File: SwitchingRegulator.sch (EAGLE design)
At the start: 31 parts, among them J1 APP_2POS_CONFIG5V_HORIZ, J2 APP_2POS_CONFIG5V_HORIZ, J3 APP_2POS_CONFIG5V_HORIZ, Q1 Q_OKI-78SR, Q2 Q_CSD18532KCSPCB

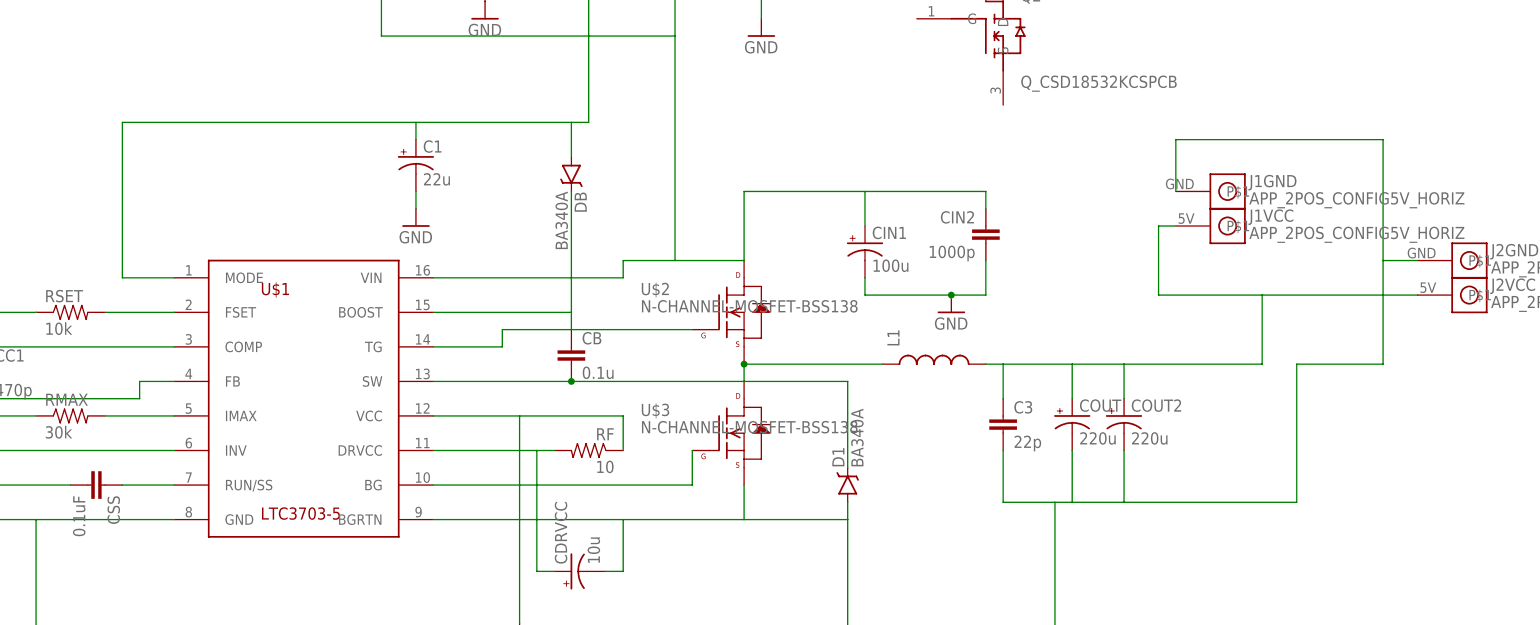
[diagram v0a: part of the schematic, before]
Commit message: Updated a few components
COUT 1, COUT 2, CIN1, and C1 now correspond to their true package
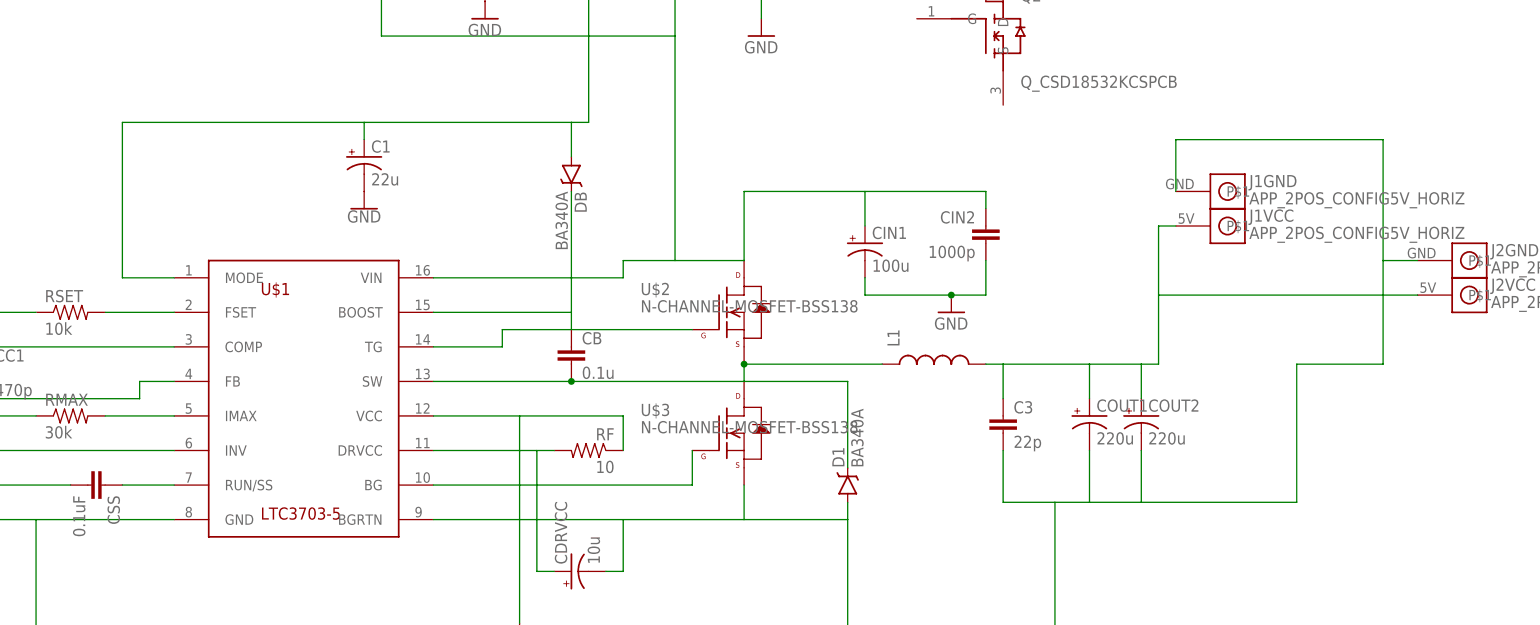
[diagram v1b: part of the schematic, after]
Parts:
- removed COUT: 220u, SparkFun-Passives:CAP_POL1206
- added COUT1: 220u, MRDT-2015-PowerBoard:EGPD101ELL221MK25H
- C1: device SparkFun-Passives:CAP_POL1206 -> buckconverter:UCZ1K220MCL1GS
- CIN1: device SparkFun-Passives:CAP_POL1206 -> MRDT-2015-PowerBoard:B41858C9107M000
- COUT2: device SparkFun-Passives:CAP_POL1206 -> MRDT-2015-PowerBoard:EGPD101ELL221MK25H
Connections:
- net GND: now also C1.-, COUT1.-; no longer COUT.-
- net VOUT12+: now also COUT1.+; no longer COUT.+
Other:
- moved on the sheet: C1, COUT2
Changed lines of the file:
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@@
 <part name="RF" library="SparkFun-Passives" deviceset="RESISTOR" device="0603-RES" value="10"/>
 <part name="GND1" library="SparkFun-Aesthetics" deviceset="GND" device=""/>
-<part name="GND2" library="SparkFun-Aesthetics" deviceset="GND" device=""/>
 <part name="GND3" library="SparkFun-Aesthetics" deviceset="GND" device=""/>
-<part name="CIN1" library="SparkFun-Passives" deviceset="CAP_POL" device="1206" value="100u"/>
-<part name="C1" library="SparkFun-Passives" deviceset="CAP_POL" device="1206" value="22u"/>
 <part name="CDRVCC" library="SparkFun-Passives" deviceset="CAP_POL" device="1206" value="10u"/>
-<part name="COUT" library="SparkFun-Passives" deviceset="CAP_POL" device="1206" value="220u"/>
-<part name="COUT2" library="SparkFun-Passives" deviceset="CAP_POL" device="1206" value="220u"/>
 <part name="GND4" library="SparkFun-Aesthetics" deviceset="GND" device=""/>
 <part name="Q1" library="MRDT-2014-All" deviceset="Q_OKI-78SR" device=""/>
@@
 <part name="J3" library="MRDT-Connectors" deviceset="APP_2POS_CONFIG" device="5V_HORIZ"/>
 <part name="Q2" library="MRDT-2014-All" deviceset="Q_CSD18532KCS" device="PCB"/>
+<part name="COUT1" library="MRDT-2015-PowerBoard" deviceset="EGPD101ELL221MK25H" device="" value="220u"/>
+<part name="COUT2" library="MRDT-2015-PowerBoard" deviceset="EGPD101ELL221MK25H" device="" value="220u"/>
+<part name="CIN1" library="MRDT-2015-PowerBoard" deviceset="B41858C9107M000" device="" value="100u"/>
+<part name="C1" library="buckconverter" deviceset="UCZ1K220MCL1GS" device="" value="22u"/>
+<part name="GND2" library="SparkFun-PowerSymbols" library_urn="urn:adsk.eagle:library:530" deviceset="GND" device=""/>
 </parts>
 <sheets>
@@
 <instance part="RF" gate="G$1" x="127" y="109.22" rot="MR0"/>
 <instance part="GND1" gate="1" x="30.48" y="73.66"/>
-<instance part="GND2" gate="1" x="101.6" y="142.24"/>
 <instance part="GND3" gate="1" x="180.34" y="129.54"/>
-<instance part="CIN1" gate="G$1" x="167.64" y="139.7"/>
-<instance part="C1" gate="G$1" x="101.6" y="152.4"/>
 <instance part="CDRVCC" gate="G$1" x="124.46" y="91.44" rot="R90"/>
-<instance part="COUT" gate="G$1" x="198.12" y="114.3"/>
-<instance part="COUT2" gate="G$1" x="205.74" y="114.3"/>
 <instance part="GND4" gate="1" x="152.4" y="170.18"/>
 <instance part="Q1" gate="G$1" x="111.76" y="187.96"/>
@@
 <instance part="J3" gate="VCC" x="139.7" y="195.58" rot="R90"/>
 <instance part="Q2" gate="G$1" x="187.96" y="170.18"/>
+<instance part="COUT1" gate="G$1" x="200.66" y="111.76"/>
+<instance part="COUT2" gate="G$1" x="208.28" y="111.76"/>
+<instance part="CIN1" gate="G$1" x="167.64" y="137.16"/>
+<instance part="C1" gate="G$1" x="93.98" y="149.86"/>
+<instance part="GND2" gate="1" x="93.98" y="144.78"/>
 </instances>
 <busses>
@@
 <wire x1="165.1" y1="99.06" x2="165.1" y2="76.2" width="0.1524" layer="91"/>
 <wire x1="165.1" y1="76.2" x2="116.84" y2="76.2" width="0.1524" layer="91"/>
-<pinref part="COUT2" gate="G$1" pin="-"/>
-<wire x1="205.74" y1="109.22" x2="205.74" y2="101.6" width="0.1524" layer="91"/>
-<wire x1="205.74" y1="101.6" x2="198.12" y2="101.6" width="0.1524" layer="91"/>
 <pinref part="C3" gate="G$1" pin="2"/>
-<wire x1="198.12" y1="101.6" x2="195.58" y2="101.6" width="0.1524" layer="91"/>
 <wire x1="195.58" y1="101.6" x2="187.96" y2="101.6" width="0.1524" layer="91"/>
 <wire x1="187.96" y1="101.6" x2="187.96" y2="109.22" width="0.1524" layer="91"/>
-<pinref part="COUT" gate="G$1" pin="-"/>
-<wire x1="198.12" y1="109.22" x2="198.12" y2="101.6" width="0.1524" layer="91"/>
 <wire x1="195.58" y1="101.6" x2="195.58" y2="76.2" width="0.1524" layer="91"/>
 <wire x1="195.58" y1="76.2" x2="165.1" y2="76.2" width="0.1524" layer="91"/>
@@
 <wire x1="132.08" y1="91.44" x2="132.08" y2="99.06" width="0.1524" layer="91"/>
 <wire x1="231.14" y1="121.92" x2="231.14" y2="101.6" width="0.1524" layer="91"/>
-<wire x1="231.14" y1="101.6" x2="205.74" y2="101.6" width="0.1524" layer="91"/>
+<wire x1="231.14" y1="101.6" x2="208.28" y2="101.6" width="0.1524" layer="91"/>
+<wire x1="208.28" y1="101.6" x2="200.66" y2="101.6" width="0.1524" layer="91"/>
+<wire x1="200.66" y1="101.6" x2="195.58" y2="101.6" width="0.1524" layer="91"/>
 <wire x1="231.14" y1="121.92" x2="243.84" y2="121.92" width="0.1524" layer="91"/>
 <wire x1="243.84" y1="121.92" x2="243.84" y2="137.16" width="0.1524" layer="91"/>
@@
 <wire x1="213.36" y1="154.94" x2="243.84" y2="154.94" width="0.1524" layer="91"/>
 <wire x1="243.84" y1="154.94" x2="243.84" y2="137.16" width="0.1524" layer="91"/>
-</segment>
-<segment>
-<pinref part="GND2" gate="1" pin="GND"/>
-<wire x1="101.6" y1="144.78" x2="101.6" y2="147.32" width="0.1524" layer="91"/>
+<pinref part="COUT1" gate="G$1" pin="-"/>
+<wire x1="200.66" y1="109.22" x2="200.66" y2="101.6" width="0.1524" layer="91"/>
+<pinref part="COUT2" gate="G$1" pin="-"/>
+<wire x1="208.28" y1="109.22" x2="208.28" y2="101.6" width="0.1524" layer="91"/>
 </segment>
 <segment>
@@
 <wire x1="180.34" y1="132.08" x2="167.64" y2="132.08" width="0.1524" layer="91"/>
 <junction x="180.34" y="132.08"/>
+<wire x1="167.64" y1="132.08" x2="167.64" y2="134.62" width="0.1524" layer="91"/>
 <pinref part="CIN1" gate="G$1" pin="-"/>
-<wire x1="167.64" y1="132.08" x2="167.64" y2="134.62" width="0.1524" layer="91"/>
 </segment>
 <segment>
@@
 <pinref part="Q1" gate="G$1" pin="GND"/>
 <pinref part="GND5" gate="1" pin="GND"/>
+</segment>
+<segment>
+<pinref part="C1" gate="G$1" pin="-"/>
+<pinref part="GND2" gate="1" pin="GND"/>
 </segment>
 </net>
@@
 <wire x1="66.04" y1="134.62" x2="58.42" y2="134.62" width="0.1524" layer="91"/>
 <wire x1="58.42" y1="134.62" x2="58.42" y2="157.48" width="0.1524" layer="91"/>
-<wire x1="58.42" y1="157.48" x2="101.6" y2="157.48" width="0.1524" layer="91"/>
-<pinref part="C1" gate="G$1" pin="+"/>
-<wire x1="101.6" y1="157.48" x2="124.46" y2="157.48" width="0.1524" layer="91"/>
-<wire x1="101.6" y1="154.94" x2="101.6" y2="157.48" width="0.1524" layer="91"/>
+<wire x1="58.42" y1="157.48" x2="93.98" y2="157.48" width="0.1524" layer="91"/>
 <pinref part="Q1" gate="G$1" pin="VOUT"/>
+<wire x1="93.98" y1="157.48" x2="124.46" y2="157.48" width="0.1524" layer="91"/>
 <wire x1="127" y1="187.96" x2="127" y2="157.48" width="0.1524" layer="91"/>
 <wire x1="127" y1="157.48" x2="124.46" y2="157.48" width="0.1524" layer="91"/>
+<pinref part="C1" gate="G$1" pin="+"/>
+<wire x1="93.98" y1="157.48" x2="93.98" y2="154.94" width="0.1524" layer="91"/>
 </segment>
 </net>
@@
 <wire x1="167.64" y1="147.32" x2="185.42" y2="147.32" width="0.1524" layer="91"/>
 <wire x1="185.42" y1="147.32" x2="185.42" y2="144.78" width="0.1524" layer="91"/>
-<pinref part="CIN1" gate="G$1" pin="+"/>
 <wire x1="167.64" y1="142.24" x2="167.64" y2="147.32" width="0.1524" layer="91"/>
 <pinref part="Q1" gate="G$1" pin="VIN"/>
@@
 <pinref part="J3" gate="VCC" pin="P$1"/>
 <wire x1="139.7" y1="187.96" x2="139.7" y2="170.18" width="0.1524" layer="91"/>
+<pinref part="CIN1" gate="G$1" pin="+"/>
 </segment>
 </net>
 <net name="VOUT12+" class="0">
 <segment>
-<pinref part="COUT" gate="G$1" pin="+"/>
-<wire x1="198.12" y1="116.84" x2="198.12" y2="121.92" width="0.1524" layer="91"/>
-<pinref part="L1" gate="G$1" pin="2"/>
-<wire x1="198.12" y1="121.92" x2="187.96" y2="121.92" width="0.1524" layer="91"/>
-<pinref part="COUT2" gate="G$1" pin="+"/>
-<wire x1="187.96" y1="121.92" x2="185.42" y2="121.92" width="0.1524" layer="91"/>
-<wire x1="205.74" y1="116.84" x2="205.74" y2="121.92" width="0.1524" layer="91"/>
-<wire x1="205.74" y1="121.92" x2="198.12" y2="121.92" width="0.1524" layer="91"/>
-<pinref part="C3" gate="G$1" pin="1"/>
-<wire x1="187.96" y1="116.84" x2="187.96" y2="121.92" width="0.1524" layer="91"/>
-<wire x1="226.06" y1="121.92" x2="205.74" y2="121.92" width="0.1524" layer="91"/>
 <pinref part="J2" gate="VCC" pin="P$1"/>
-<wire x1="248.92" y1="132.08" x2="226.06" y2="132.08" width="0.1524" layer="91"/>
-<wire x1="226.06" y1="132.08" x2="226.06" y2="121.92" width="0.1524" layer="91"/>
-<wire x1="226.06" y1="132.08" x2="210.82" y2="132.08" width="0.1524" layer="91"/>
+<wire x1="248.92" y1="132.08" x2="210.82" y2="132.08" width="0.1524" layer="91"/>
 <wire x1="210.82" y1="132.08" x2="210.82" y2="142.24" width="0.1524" layer="91"/>
 <pinref part="J1" gate="VCC" pin="P$1"/>
 <wire x1="210.82" y1="142.24" x2="213.36" y2="142.24" width="0.1524" layer="91"/>
+<pinref part="L1" gate="G$1" pin="2"/>
+<wire x1="210.82" y1="121.92" x2="208.28" y2="121.92" width="0.1524" layer="91"/>
+<pinref part="COUT2" gate="G$1" pin="+"/>
+<wire x1="208.28" y1="116.84" x2="208.28" y2="121.92" width="0.1524" layer="91"/>
+<wire x1="208.28" y1="121.92" x2="200.66" y2="121.92" width="0.1524" layer="91"/>
+<pinref part="COUT1" gate="G$1" pin="+"/>
+<wire x1="200.66" y1="116.84" x2="200.66" y2="121.92" width="0.1524" layer="91"/>
+<wire x1="200.66" y1="121.92" x2="187.96" y2="121.92" width="0.1524" layer="91"/>
+<wire x1="187.96" y1="121.92" x2="185.42" y2="121.92" width="0.1524" layer="91"/>
+<pinref part="C3" gate="G$1" pin="1"/>
+<wire x1="187.96" y1="116.84" x2="187.96" y2="121.92" width="0.1524" layer="91"/>
+<wire x1="210.82" y1="121.92" x2="210.82" y2="132.08" width="0.1524" layer="91"/>
 </segment>
 </net>
@@
 </schematic>
 </drawing>
+<compatibility>
+<note version="8.2" severity="warning">
+Since Version 8.2, EAGLE supports online libraries. The ids
+of those online libraries will not be understood (or retained)
+with this version.
+</note>
+<note version="8.3" severity="warning">
+Since Version 8.3, EAGLE supports URNs for individual library
+assets (packages, symbols, and devices). The URNs of those assets
+will not be understood (or retained) with this version.
+</note>
+</compatibility>
 </eagle>
